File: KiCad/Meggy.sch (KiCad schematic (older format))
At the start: 23 parts, among them J1 USB_B_Micro, J2 Conn_01x03, SW1 SW_Push, SW2 SW_Push, U1 ROM-socket-42pin, U2 AT90USB1286-MU, U3 M29F160F, U4 74AHCT1G126GW,125, X1 Standard_Clock_Oscillators_XT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

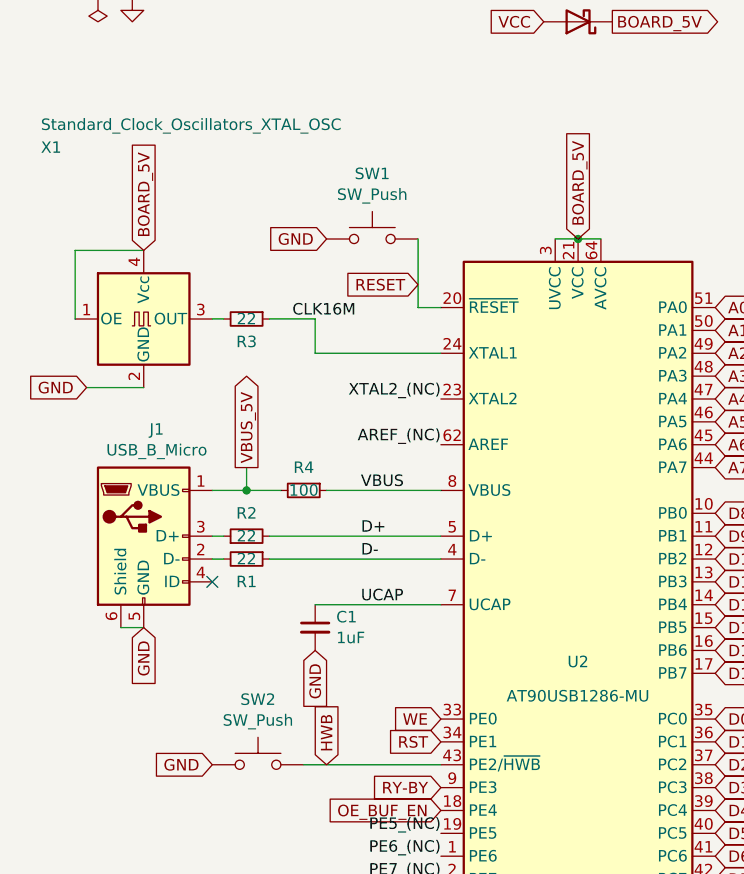
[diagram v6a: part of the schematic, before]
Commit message: Removed RESET-button
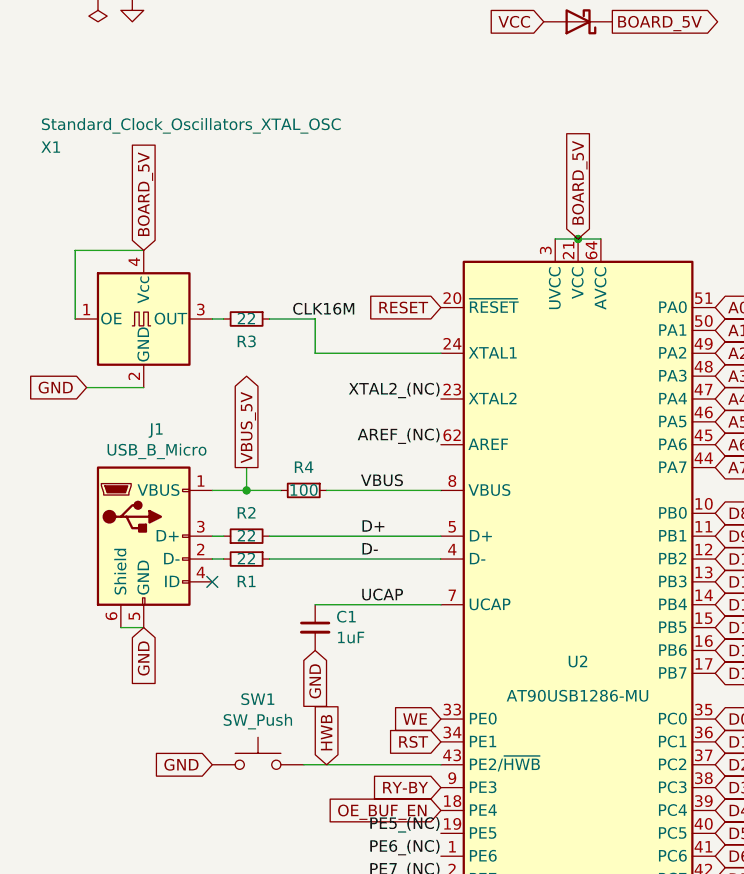
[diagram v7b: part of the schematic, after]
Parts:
- removed SW1: SW_Push, Meggy:Sunrom_Tactile_Switch_3x4x2mm_SMD_2-Pin, symbol Switch:SW_Push
- renumbered SW2 to SW1
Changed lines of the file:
@@
 Text GLabel 2550 5450 0    50   Input ~ 0
 A18
-Text GLabel 2450 2450 0    50   Input ~ 0
+Text GLabel 2550 2550 0    50   Input ~ 0
 RESET
 Text GLabel 2050 4550 1    50   Input ~ 0
@@
 $Comp
 L Switch:SW_Push SW1
-U 1 1 68D03EF3
-P 2250 2250
-F 0 "SW1" H 2250 2535 50  0000 C CNN
-F 1 "SW_Push" H 2250 2444 50  0000 C CNN
-F 2 "Meggy:Sunrom_Tactile_Switch_3x4x2mm_SMD_2-Pin" H 2250 2450 50  0001 C CNN
-F 3 "~" H 2250 2450 50  0001 C CNN
-	1    2250 2250
-	1    0    0    -1
-$EndComp
-Text GLabel 2050 2250 0    50   Input ~ 0
-GND
-Wire Wire Line
-	2550 2550 2450 2550
-Wire Wire Line
-	2450 2550 2450 2250
-$Comp
-L Switch:SW_Push SW2
 U 1 1 68D65985
 P 1750 4550
-F 0 "SW2" H 1750 4835 50  0000 C CNN
+F 0 "SW1" H 1750 4835 50  0000 C CNN
 F 1 "SW_Push" H 1750 4744 50  0000 C CNN
 F 2 "Meggy:Sunrom_Tactile_Switch_3x4x2mm_SMD_2-Pin" H 1750 4750 50  0001 C CNN

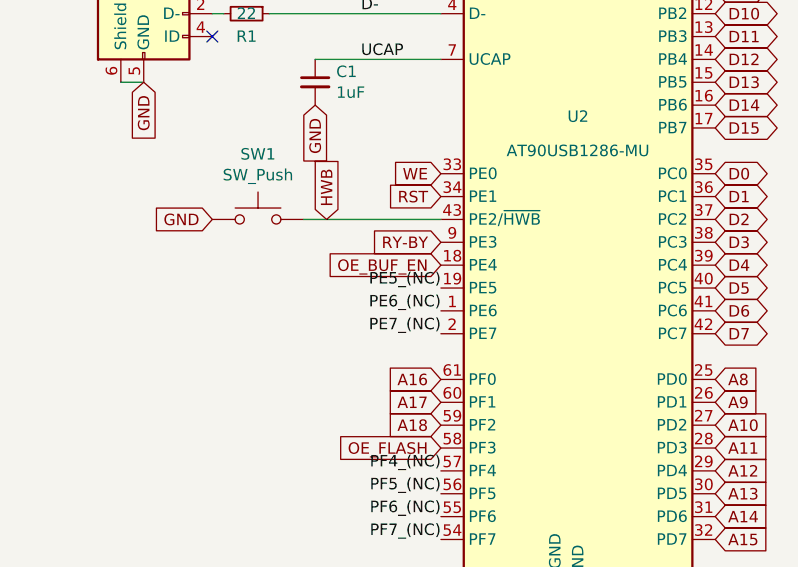
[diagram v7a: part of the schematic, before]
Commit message: Rev C: connect PE5 (pin 19) to /RESET (pin 20) for software DFU entry via --avr-reset
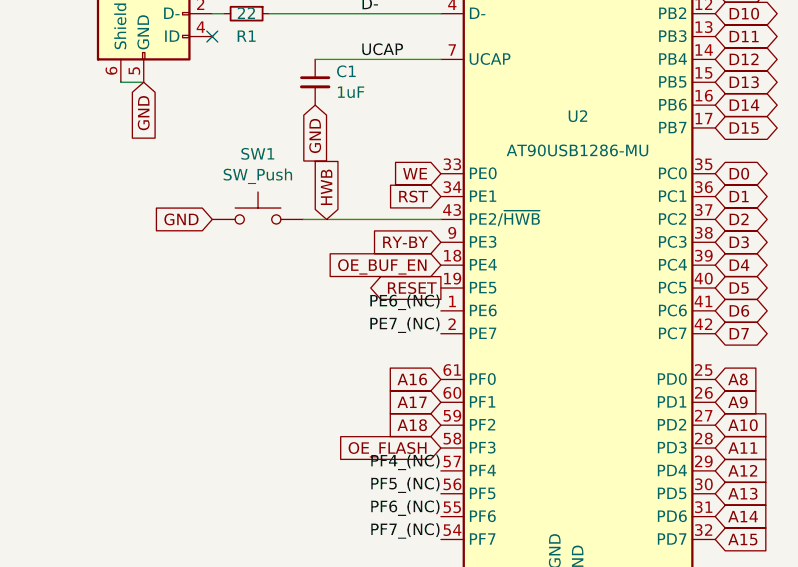
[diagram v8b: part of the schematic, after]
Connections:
- net PE5_(NC) is gone; now on net RESET: U2.19 (PE5)
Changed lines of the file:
@@
 Text Label 2550 3150 2    50   ~ 0
 AREF_(NC)
-Text Label 2550 4850 2    50   ~ 0
-PE5_(NC)
 Text Label 2550 4950 2    50   ~ 0
 PE6_(NC)
@@
 Text GLabel 3300 1300 2    50   Output ~ 0
 BOARD_5V
+Text GLabel 2550 4850 0    50   Output ~ 0
+RESET
 $EndSCHEMATC
